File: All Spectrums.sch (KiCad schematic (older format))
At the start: 7 parts

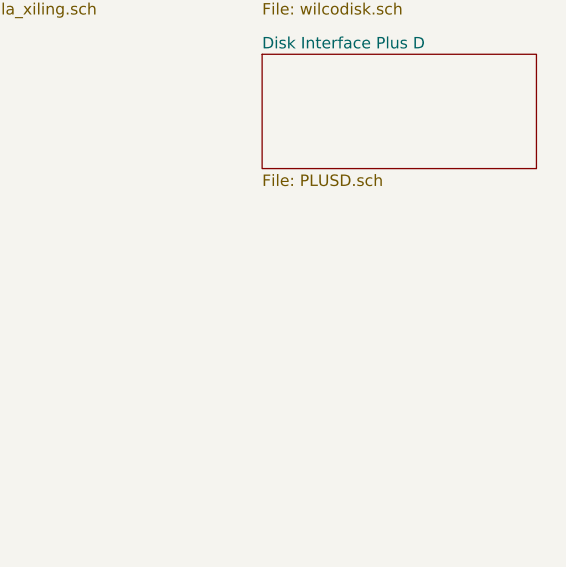
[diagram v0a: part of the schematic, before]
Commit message: add plus 3 disk interface
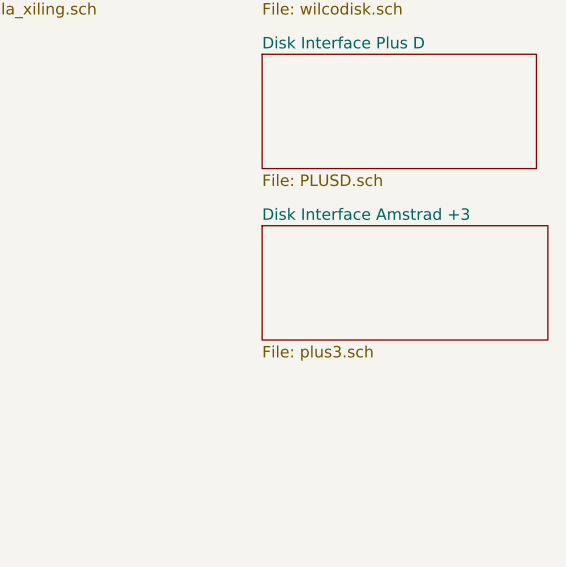
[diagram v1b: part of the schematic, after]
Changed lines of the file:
@@
 $Descr A4 11693 8268
 encoding utf-8
-Sheet 1 16
+Sheet 1 17
 Title ""
 Date ""
@@
 F1 "memoria_rom.sch" 50
 $EndSheet
+$Sheet
+S 6150 3150 1250 500
+U 5BC4D98A
+F0 "Disk Interface Amstrad +3" 50
+F1 "plus3.sch" 50
+$EndSheet
 $EndSCHEMATC
